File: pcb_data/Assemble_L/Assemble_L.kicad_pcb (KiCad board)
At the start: 2 copper layers, 158.4 x 96.4 mm, 84 parts, among them J1 Conn_01x02, U1 XIAO-nRF52840

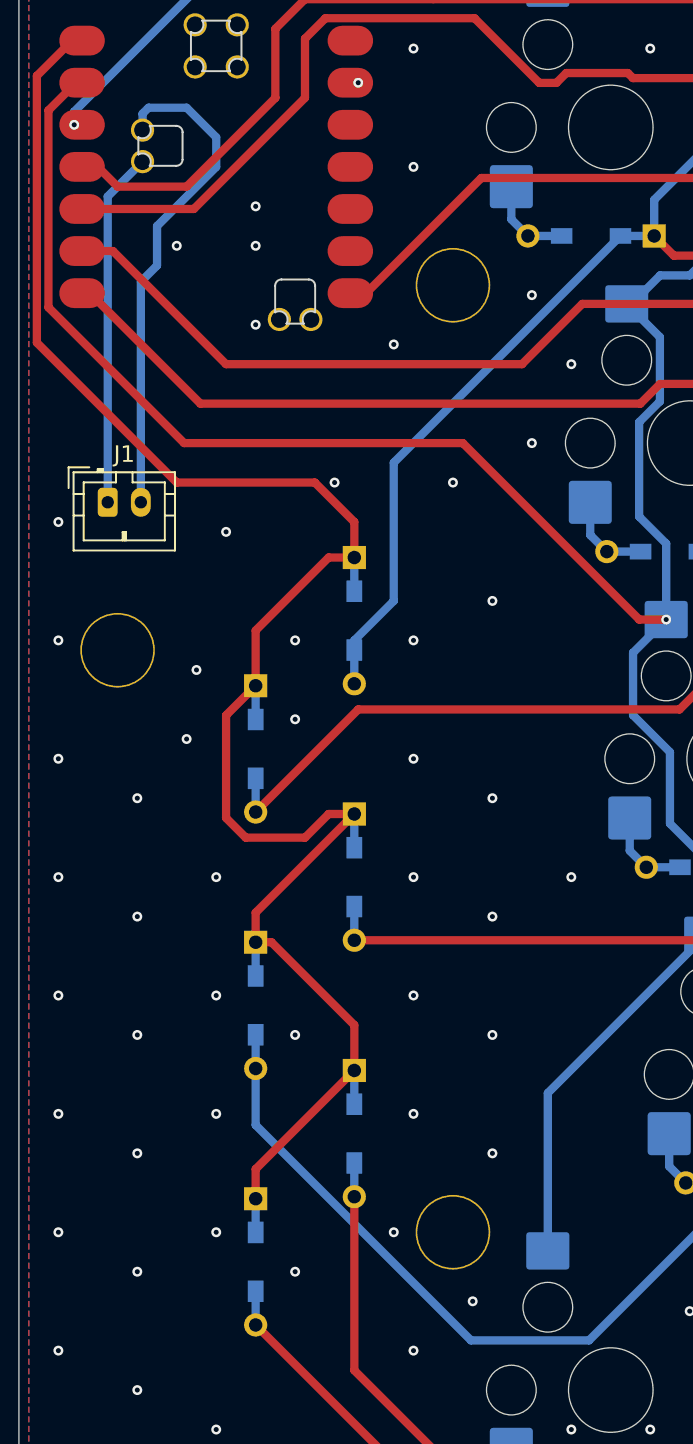
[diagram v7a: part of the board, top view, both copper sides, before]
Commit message: Issue/21 add capacitor bat gnd (#23)
* add Capacitor symbol

* add Capacitor foot print

* project file updated

* add model number of capacitor
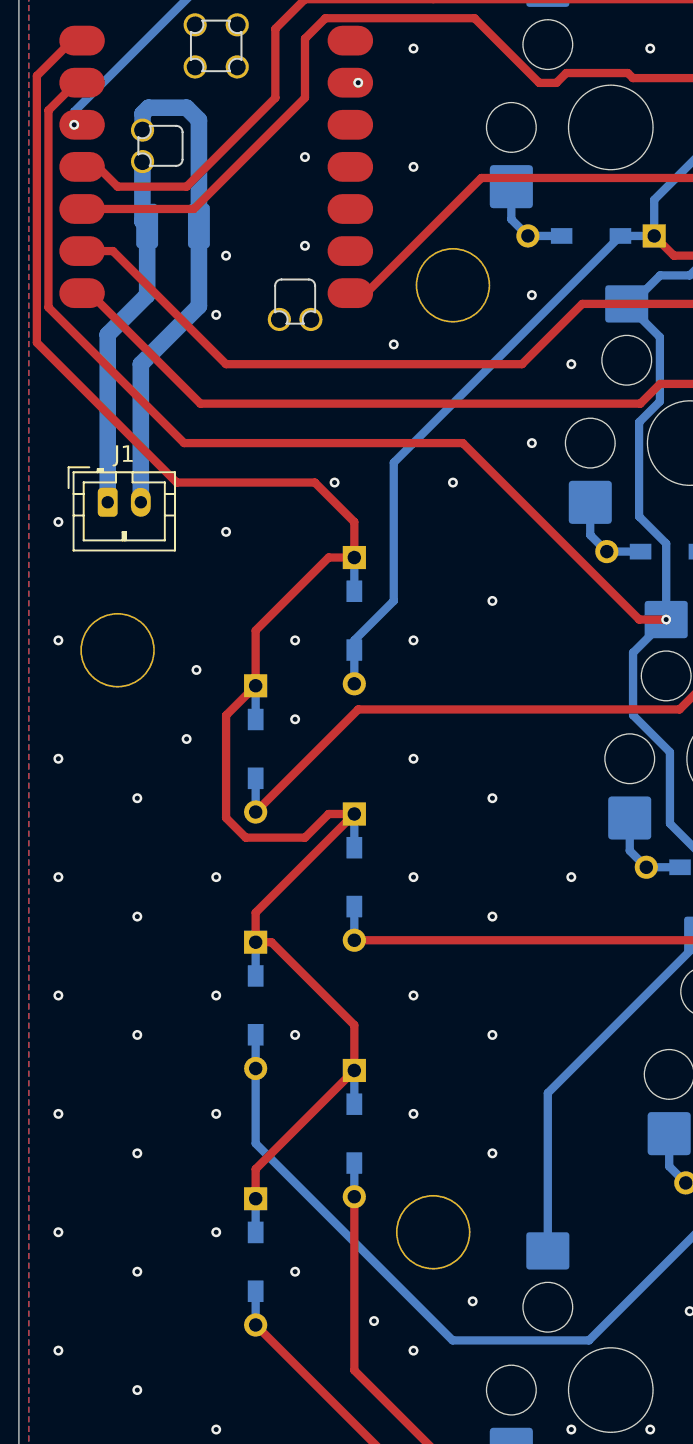
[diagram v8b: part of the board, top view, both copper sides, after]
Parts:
- added C1: C, Capacitor_SMD:C_1210_3225Metric_Pad1.33x2.70mm_HandSolder, B.Cu at (54.5, 63.1)
- moved H4 1.19 mm to (70.2, 123.8)
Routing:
- net GND: track 30.2 -> 29.4 mm
- net Net-(D0-3-K): track 213.5 -> 214.1 mm
